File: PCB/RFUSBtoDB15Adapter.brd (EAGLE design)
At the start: 39 x 66 mm, 7 parts, among them J2 AVR_SPI_PROG_3X2NS

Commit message: New PCB
PCB updated
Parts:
- added C1: 0.1uf, Wurth_Elektronik_Passive_Capacitors_rev18b:WCAP-CSGP_0805_REFLOW
- added C2: 10uF, SparkFun-Capacitors:EIA3216
- added IC1: S-816A40AMC-BAPT2U, S-816A40AMC-BAPT2U:SOT95P275X130-5N
- added JP2: (no value), pinhead:1X01
- added LED: (no value), adafruit:LED3MM
- added PEM1, PEM2, PEM3, PEM4: KF2-M2, penn-engineering:KF2-M2
- added Q2: 2SA1213-Y(TE12L,F), 2SA1213YTE12LF:PW-MINI_TOS
- added R1: 33Ω, eagle-ltspice:R0805
- added SJ1, SJ2, SJ3: (no value), jumper:SJ
- moved 3.3V 3.81 mm to (38.1, 57.1)
- moved J2 3.81 mm to (8.89, 20.3)
- moved ARDUINO-ATMEGA328P 3.81 mm to (24.1, 38.1)
- moved DB15OUT 3.81 mm to (23.4, 71.2)
- moved JP3 3.81 mm to (21.6, 22.9)
- moved J1 3.81 mm to (36.8, 16.5)
- moved JP1 3.81 mm to (37.8, 64.1)
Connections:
- new net 5VREG: 3.3V.3, C1.1, C2.+, IC1.3, IC1.5, JP1.1, Q2.3, R1.2, SJ1.2, SJ3.1, SJ3.2
- new net BASE: IC1.1, Q2.1
- new net VBUS: C1.2, JP2.1, R1.1
- net 5VSG: now also IC1.4, Q2.2, SJ1.1, SJ2.1, SJ2.2; no longer 3.3V.3, J2.2, JP1.1
- net GND: now also C2.-, IC1.2
- net VCCIN: now also J2.2
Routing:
- net 5VREG: track 0.00 -> 142.7 mm
- net 5VSG: track 93.3 -> 28.0 mm, vias 3 -> 0
- net VCCIN: track 58.8 -> 93.3 mm
- net BASE: track 0.00 -> 28.1 mm
- net VBUS: track 0.00 -> 7.99 mm, vias 0 -> 1
- net BUT3: track 70.1 -> 74.2 mm
- net START: track 43.6 -> 41.0 mm
- net UP: track 62.5 -> 61.2 mm
- net BUT6: track 31.5 -> 32.5 mm
- net DOWN: track 39.1 -> 38.5 mm
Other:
- board size 39 x 66 mm -> 52.1 x 68.6 mm
- board text added: "For instructions access: github.com/Raphfriend/USB2DB15"
- board text removed: "https://github.com/Raphfriend/USB2DB15"

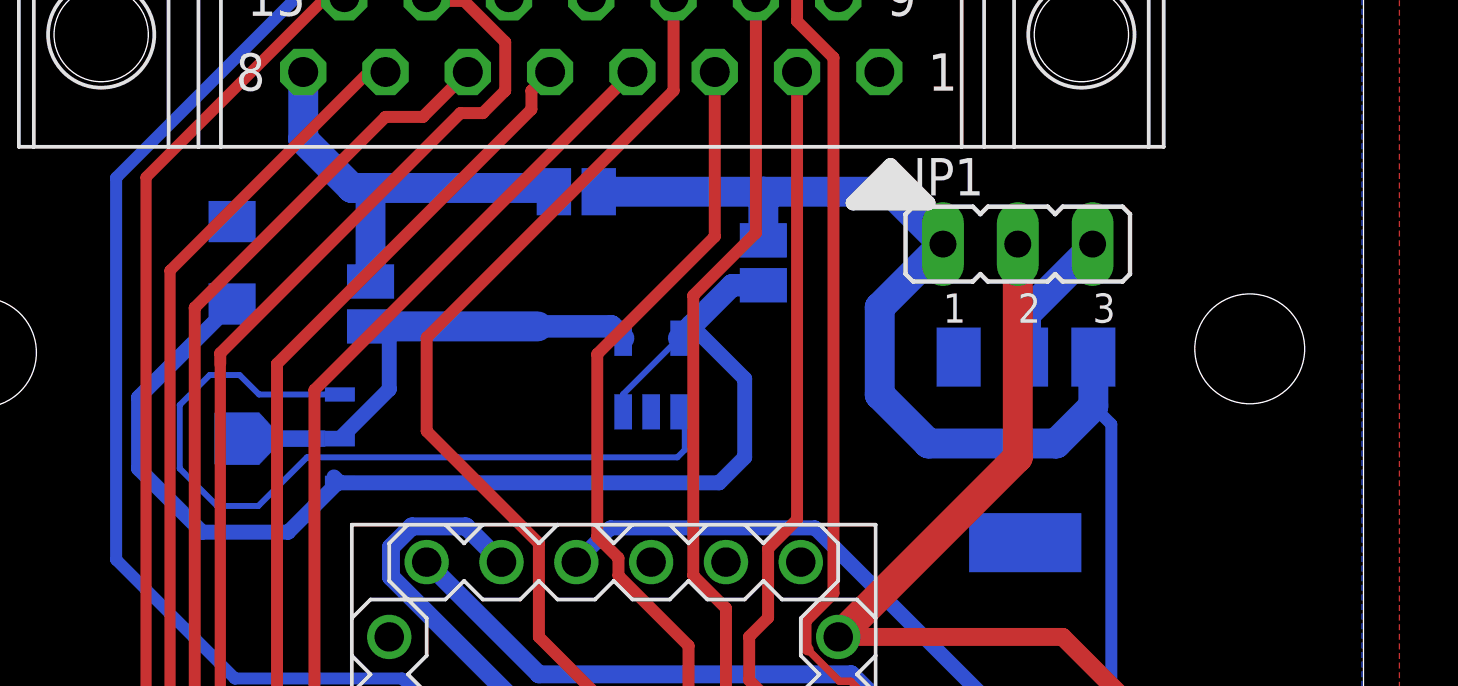
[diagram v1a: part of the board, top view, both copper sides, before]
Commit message: Update RFUSBtoDB15Adapter.brd
Changes on PCB
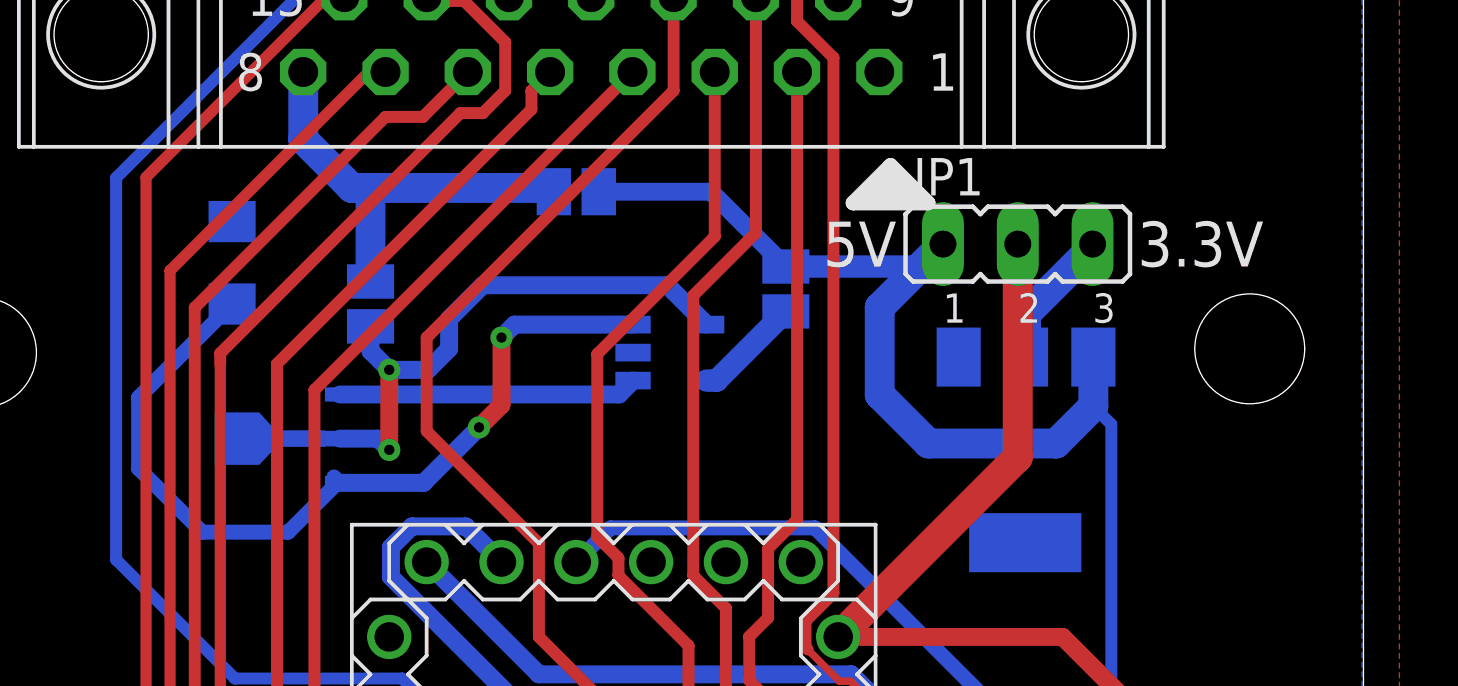
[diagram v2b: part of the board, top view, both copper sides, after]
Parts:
- moved SJ3 1.17 mm to (30.0, 62.6)
- moved IC1 0.99 mm to (26.0, 60.5), turned to 180 degrees
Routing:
- net BASE: track 28.1 -> 10.1 mm
- net 5VREG: track 142.7 -> 132.2 mm, vias 0 -> 2
- net 5VSG: track 28.0 -> 34.1 mm, vias 0 -> 2
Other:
- board text added: "3.3V"
- board text added: "5V"

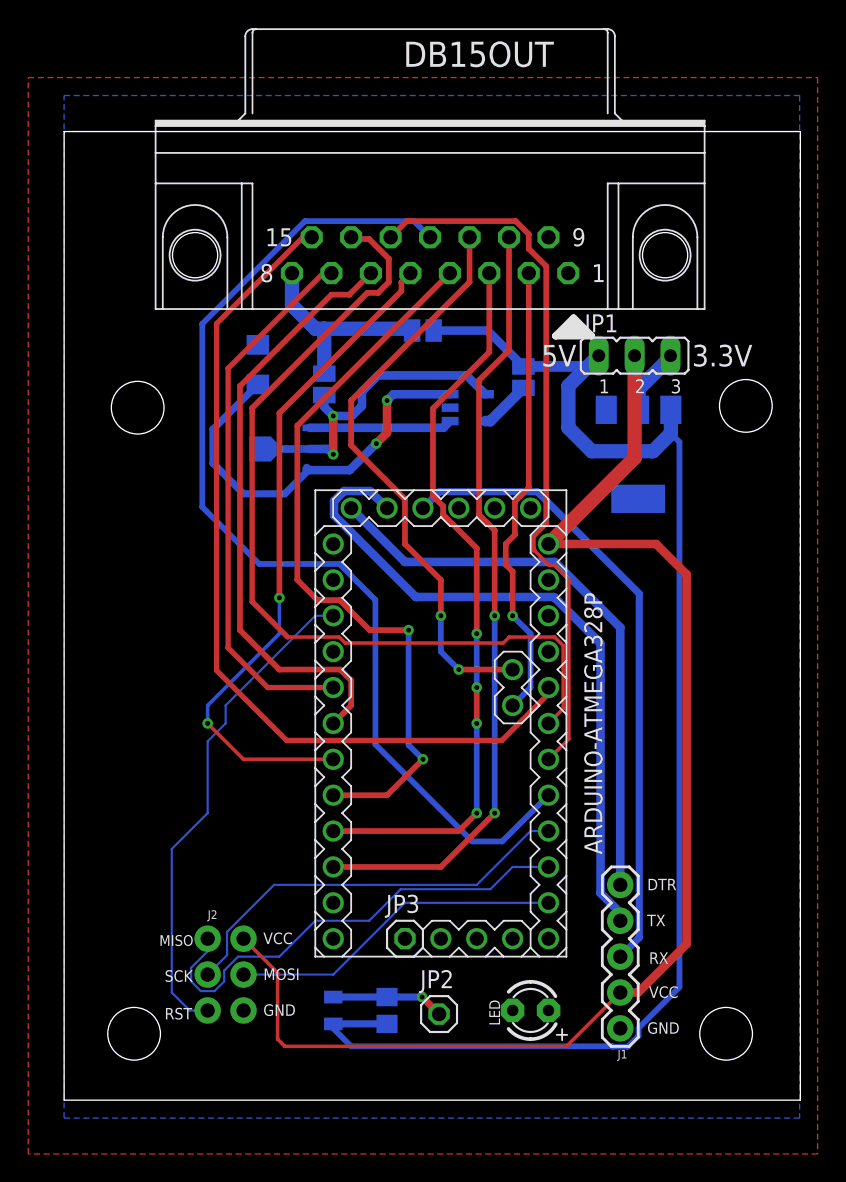
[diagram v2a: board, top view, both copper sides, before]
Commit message: Updates
Schematic, PCB and code updates.
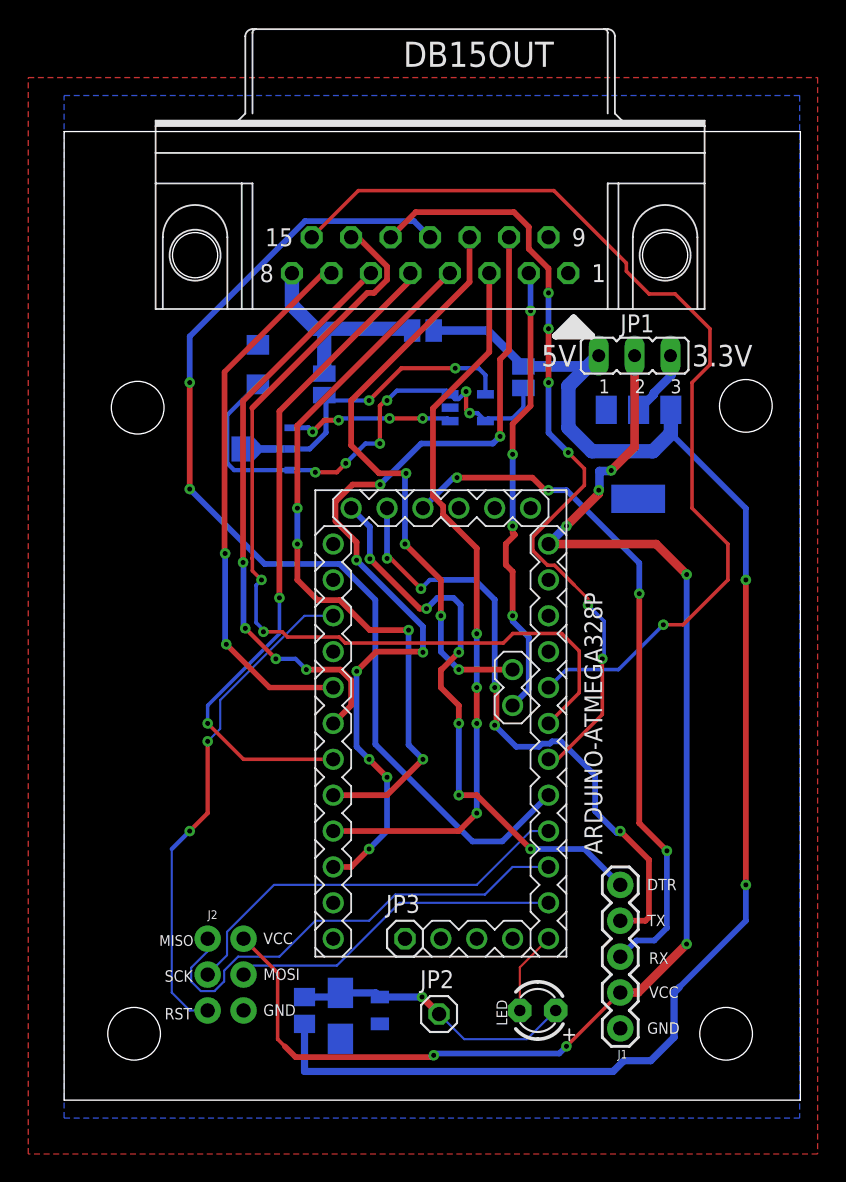
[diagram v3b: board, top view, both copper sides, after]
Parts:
- added C5: 4.7UF, resistor:B/3528-21W
- DB15OUT, J1, JP3: value (none) -> 0
- JP2: value (none) -> JP2
- moved R1 5.84 mm to (14.5, 17.8)
- moved C1 3.30 mm to (19.8, 17.8)
- moved Q2 1.27 mm to (11.8, 57.5)
- moved LED 0.51 mm to (31.0, 17.8)
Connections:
- new net LED: ARDUINO-ATMEGA328P.J6.12, LED.K
- new net VCC: ARDUINO-ATMEGA328P.J6.4
- net 5VREG: no longer C1.1
- net GND: now also C1.1, C5.-
- net VBUS: now also C5.+, LED.A
- net VCCIN: no longer ARDUINO-ATMEGA328P.J6.4
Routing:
- net VBUS: track 7.99 -> 20.1 mm
- net 5VREG: track 132.2 -> 141.9 mm, vias 2 -> 8
- net BUT5: track 55.1 -> 63.5 mm, vias 2 -> 8
- net UP: track 61.2 -> 69.2 mm, vias 0 -> 1
- net LED: track 0.00 -> 5.92 mm
- net BUT1: track 50.6 -> 56.2 mm, vias 0 -> 6
- net RX: track 45.0 -> 49.5 mm, vias 0 -> 4
- net TX: track 48.4 -> 44.9 mm, vias 0 -> 5
- net BASE: track 10.1 -> 11.8 mm, vias 0 -> 4
- net LEFT: track 62.0 -> 63.6 mm, vias 0 -> 2
- net START: track 41.0 -> 42.2 mm, vias 2 -> 4
- net RIGHT: track 42.8 -> 41.8 mm, vias 0 -> 4
- net VCCIN: track 93.3 -> 94.1 mm, vias 0 -> 7
- net BUT3: track 74.2 -> 74.8 mm, vias 0 -> 2
- net DTR: track 40.8 -> 41.2 mm, vias 0 -> 6
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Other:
- board text added: "+"
- board text added: "4.7uf"
- board text added: "USB2DB15 Adapter for Supergun/Neogeo 1.0 by Raph_friend"
- board text removed: "USB2DB15 Adapter for Supergun/Neogeo"
- board text removed: "by Raph_friend"

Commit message: PCB
Some changes
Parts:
- added LOGO1: OSHW-LOGOS, SparkFun-Aesthetics:OSHW-LOGO-S
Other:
- board text added: "Made in Brazil"
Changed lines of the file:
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@@
 <text x="18.415" y="19.558" size="0.6096" layer="26" rot="MR0">+</text>
 <text x="12.446" y="60.579" size="0.6096" layer="26" rot="MR0">+</text>
+<text x="25.146" y="41.91" size="1.778" layer="26" rot="MR270">Made in Brazil</text>
 </plain>
 <attributes>
@@
 <attribute name="VALUE" x="14.093" y="15.449" size="1.27" layer="28" rot="MR90"/>
 </element>
+<element name="LOGO1" library="SparkFun-Aesthetics" library_urn="urn:adsk.eagle:library:507" package="OSHW-LOGO-S" package3d_urn="urn:adsk.eagle:package:37099/1" value="OSHW-LOGOS" x="0.381" y="55.372" smashed="yes" rot="MR90"/>
 </elements>
 <signals>

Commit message: PCB
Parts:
- added S1: RS032G05A3SM-SPST-MOMENTARY-SWSMD-1101NE, BeagleBone_Blue_R3:TACTILE-SWITCH-1101NE
- renumbered JP3 to A4
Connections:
- net BUT6: now also A4.1
- net GND: now also S1.1; no longer ARDUINO-ATMEGA328P.J3.1
- net RESET: now also S1.2
- net START: now also ARDUINO-ATMEGA328P.J3.1
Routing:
- net START: track 42.2 -> 68.9 mm
- net BUT6: track 32.7 -> 56.0 mm
- net RESET: track 35.7 -> 40.8 mm
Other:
- board text added: "A4"
- board text added: "A5"
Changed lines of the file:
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@@
 <text x="12.446" y="60.579" size="0.6096" layer="26" rot="MR0">+</text>
 <text x="25.146" y="41.91" size="1.778" layer="26" rot="MR270">Made in Brazil</text>
+<text x="22.987" y="24.257" size="1.27" layer="25">A5</text>
+<text x="30.353" y="44.577" size="1.27" layer="25" rot="R180">A5</text>
+<text x="30.353" y="37.973" size="1.27" layer="25" rot="R180">A4</text>
 </plain>
 <attributes>
@@
 <attribute name="VALUE" x="4.953" y="24.13" size="0.6096" layer="27" font="vector" ratio="20" rot="R270"/>
 </element>
-<element name="JP3" library="pinhead" library_urn="urn:adsk.eagle:library:325" package="1X01" package3d_urn="urn:adsk.eagle:package:22485/2" value="0" x="21.59" y="22.86" smashed="yes">
-<attribute name="NAME" x="20.2438" y="24.6888" size="1.27" layer="25" ratio="10"/>
+<element name="A4" library="pinhead" library_urn="urn:adsk.eagle:library:325" package="1X01" package3d_urn="urn:adsk.eagle:package:22485/2" value="0" x="21.59" y="22.86" smashed="yes">
+<attribute name="NAME" x="20.4978" y="24.3078" size="1.27" layer="25" ratio="10"/>
 <attribute name="POPULARITY" value="64" x="21.59" y="22.86" size="1.778" layer="27" display="off"/>
 <attribute name="VALUE" x="20.32" y="19.685" size="1.27" layer="27"/>
@@
 </element>
 <element name="LOGO1" library="SparkFun-Aesthetics" library_urn="urn:adsk.eagle:library:507" package="OSHW-LOGO-S" package3d_urn="urn:adsk.eagle:package:37099/1" value="OSHW-LOGOS" x="0.381" y="55.372" smashed="yes" rot="MR90"/>
+<element name="S1" library="BeagleBone_Blue_R3" library_urn="urn:adsk.eagle:library:5828899" package="TACTILE-SWITCH-1101NE" package3d_urn="urn:adsk.eagle:package:5829833/3" value="RS032G05A3SM-SPST-MOMENTARY-SWSMD-1101NE" x="3.81" y="43.18" smashed="yes" rot="R270">
+<attribute name="NAME" x="5.81" y="46.18" size="0.762" layer="25" rot="R270"/>
+<attribute name="PROD_ID" value="SWCH-00815" x="3.81" y="43.18" size="1.778" layer="27" rot="R270" display="off"/>
+<attribute name="VALUE" x="1.11" y="46.18" size="0.762" layer="27" rot="R270"/>
+</element>
 </elements>
 <signals>
@@
 <wire x1="21.664375" y1="55.805625" x2="19.759375" y2="55.805625" width="0.4064" layer="1"/>
 <wire x1="19.759375" y1="55.805625" x2="17.78" y2="57.785" width="0.4064" layer="1"/>
+<contactref element="ARDUINO-ATMEGA328P" pad="J3.1"/>
+<wire x1="24.13" y1="22.86" x2="27.7034" y2="26.4334" width="0.254" layer="1"/>
+<wire x1="27.7034" y1="26.4334" x2="31.704859375" y2="26.4334" width="0.254" layer="1"/>
+<wire x1="31.704859375" y1="26.4334" x2="32.783403125" y2="27.51194375" width="0.254" layer="1"/>
+<wire x1="32.783403125" y1="27.51194375" x2="32.783403125" y2="30.90805625" width="0.254" layer="1"/>
+<wire x1="32.783403125" y1="30.90805625" x2="31.704859375" y2="31.9866" width="0.254" layer="1"/>
+<wire x1="31.704859375" y1="31.9866" x2="31.321940625" y2="31.9866" width="0.254" layer="1"/>
+<wire x1="31.321940625" y1="31.9866" x2="30.48" y2="32.828540625" width="0.254" layer="1"/>
+<wire x1="30.48" y1="32.828540625" x2="30.48" y2="40.64" width="0.254" layer="1"/>
+<wire x1="30.48" y1="40.64" x2="29.21" y2="41.91" width="0.254" layer="1"/>
 </signal>
 <signal name="BUT4">
@@
 <via x="29.21" y="57.15" extent="1-16" drill="0.35"/>
 <wire x1="29.21" y1="57.15" x2="29.21" y2="59.309" width="0.4064" layer="1"/>
+<contactref element="A4" pad="1"/>
+<wire x1="21.59" y1="22.86" x2="27.0980625" y2="28.3680625" width="0.254" layer="1"/>
+<wire x1="27.0980625" y1="28.3680625" x2="30.5680625" y2="28.3680625" width="0.254" layer="1"/>
+<wire x1="30.5680625" y1="28.3680625" x2="31.1376" y2="28.9376" width="0.254" layer="1"/>
+<wire x1="31.1376" y1="28.9376" x2="31.1376" y2="29.5480875" width="0.254" layer="1"/>
+<wire x1="31.1376" y1="29.5480875" x2="29.21" y2="31.4756875" width="0.254" layer="1"/>
+<wire x1="29.21" y1="31.4756875" x2="29.21" y2="39.37" width="0.254" layer="1"/>
 </signal>
 <signal name="GND">
 <contactref element="DB15OUT" pad="1"/>
 <contactref element="3.3V" pad="1"/>
-<contactref element="ARDUINO-ATMEGA328P" pad="J3.1"/>
 <contactref element="J1" pad="1"/>
 <contactref element="ARDUINO-ATMEGA328P" pad="J1.1"/>
@@
 <contactref element="C1" pad="1"/>
 <contactref element="C5" pad="-"/>
+<contactref element="S1" pad="1"/>
 </signal>
 <signal name="5VSG">
@@
 <wire x1="7.62" y1="31.75" x2="7.62" y2="36.83" width="0.3048" layer="1"/>
 <via x="7.62" y="36.83" extent="1-16" drill="0.35"/>
+<contactref element="S1" pad="2"/>
+<wire x1="7.62" y1="36.83" x2="7.01" y2="36.83" width="0.1524" layer="1"/>
+<wire x1="7.01" y1="36.83" x2="3.81" y2="40.03" width="0.1524" layer="1"/>
 </signal>
 <signal name="SCK">

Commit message: PCB
PCB design updated
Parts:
- removed JP1: (no value), jumper:JP2
- removed SJ3: (no value), jumper:SJ
- added C3, C4: 10uF, SparkFun-Capacitors:EIA3216
- R1: value 33Ω -> 80R; device eagle-ltspice:R0805 -> SparkFun-Resistors:0805
- moved J1 45.2 mm to (8.89, 52.1)
- moved S1 38.9 mm to (41.9, 35.6)
- moved J2 29.9 mm to (38.7, 21.2)
- moved Q2 21.9 mm to (22.9, 38.6), turned to 180 degrees
- moved C1 16.0 mm to (24.4, 33.1)
- moved C5 16.0 mm to (21.6, 32.8)
- moved C2 14.3 mm to (25.4, 62.0), turned to 180 degrees
- moved IC1 14.1 mm to (25.9, 46.4), turned to 90 degrees
- moved R1 13.7 mm to (27.9, 15.2), turned to 0 degrees
- moved PEM2 1.02 mm to (45.3, 16.0)
- moved PEM3 0.90 mm to (1.78, 60.3)
- moved PEM1 0.80 mm to (1.65, 15.9)
- moved PEM4 0.52 mm to (45.2, 60.5)
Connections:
- removed net VBUS: C1.2, C5.+, JP2.1, LED.A, R1.1
- removed net VCC: ARDUINO-ATMEGA328P.J6.4
- removed net VCCIN: ARDUINO-ATMEGA328P.J6.1, J1.2, J2.2, JP1.2
- new net 5VLED: LED.A, R1.1
- new net RAW: ARDUINO-ATMEGA328P.J6.1
- net 3.3V: now also ARDUINO-ATMEGA328P.J6.4, C4.+; no longer JP1.3
- net 5VREG: now also C1.2, C3.+, C5.+, J1.2, J2.2, JP2.1; no longer JP1.1, SJ3.1, SJ3.2
- net GND: now also C3.-, C4.-
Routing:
- net VCCIN: track 94.1 -> 0.00 mm, vias 7 -> 0
- net RX: track 49.5 -> 15.5 mm, vias 4 -> 1
- net TX: track 44.9 -> 15.2 mm, vias 5 -> 1
- net BUT3: track 74.8 -> 46.6 mm, vias 2 -> 0
- net DTR: track 41.2 -> 14.8 mm, vias 6 -> 1
- net MISO: track 33.2 -> 8.79 mm
- net VBUS: track 20.1 -> 0.00 mm, vias 1 -> 0
- net CREDIT: track 51.8 -> 69.9 mm, vias 4 -> 2
- net 3.3V: track 4.82 -> 22.7 mm
- net SCK: track 29.3 -> 11.6 mm
- net LEFT: track 63.6 -> 48.7 mm, vias 2 -> 1
- net START: track 68.9 -> 54.7 mm, vias 4 -> 1
- net MOSI: track 23.8 -> 9.99 mm
- net GND: track 0.00 -> 13.4 mm, vias 0 -> 5
- net 5VSG: track 34.2 -> 47.1 mm, vias 2 -> 3
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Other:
- board text removed: "3.3V"
- board text removed: "5V"

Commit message: PCB update
Small changes
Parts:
- moved JP2 9.30 mm to (19.1, 25.4)
- renumbered ARDUINO-ATMEGA328P to ARDUINO-MINIPRO
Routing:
- net 5VREG: track 143.4 -> 145.3 mm
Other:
- board text added: "ARDUINO PRO MINI"
- board text added: "RESET"
- board text removed: "RST"

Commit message: PCB Update
LED status and MEMORY RESET now supported
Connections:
- new net RESET_MEM: ARDUINO-MINIPRO.J3.2, S1.2
- net LED: now also ARDUINO-MINIPRO.J7.2; no longer ARDUINO-MINIPRO.J6.12
- net RESET: no longer S1.2
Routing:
- net RESET_MEM: track 0.00 -> 20.7 mm, vias 0 -> 2
- net RESET: track 48.9 -> 47.1 mm
- net LED: track 5.92 -> 4.65 mm
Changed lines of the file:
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@@
 <drawing>
 <settings>
-<setting alwaysvectorfont="yes"/>
+<setting alwaysvectorfont="no"/>
 <setting verticaltext="up"/>
 </settings>
@@
 <contactref element="ARDUINO-MINIPRO" pad="J7.10"/>
 <contactref element="J2" pad="5"/>
-<contactref element="S1" pad="2"/>
 <via x="39.37" y="33.02" extent="1-16" drill="0.35"/>
 <wire x1="32.19909375" y1="31.9358" x2="31.30090625" y2="31.9358" width="0.3556" layer="16"/>
@@
 <wire x1="39.37" y1="29.21" x2="40.64" y2="30.48" width="0.3556" layer="16"/>
 <via x="40.64" y="30.48" extent="1-16" drill="0.35"/>
-<wire x1="41.91" y1="31.75" x2="40.64" y2="30.48" width="0.3556" layer="1"/>
-<wire x1="39.37" y1="33.02" x2="40.64" y2="33.02" width="0.3556" layer="1"/>
-<wire x1="40.64" y1="33.02" x2="41.91" y2="31.75" width="0.3556" layer="1"/>
-<wire x1="40.64" y1="30.48" x2="41.91" y2="32.41" width="0" layer="19" extent="1-1"/>
+<wire x1="40.64" y1="30.48" x2="39.37" y2="31.75" width="0.3556" layer="1"/>
+<wire x1="39.37" y1="31.75" x2="39.37" y2="33.02" width="0.3556" layer="1"/>
 </signal>
 <signal name="SCK">
@@
 </signal>
 <signal name="LED">
-<contactref element="ARDUINO-MINIPRO" pad="J6.12"/>
 <contactref element="LED" pad="K"/>
 <wire x1="29.718" y1="17.78" x2="29.718" y2="19.558" width="0.3556" layer="1"/>
 <wire x1="29.718" y1="19.558" x2="31.75" y2="21.59" width="0.3556" layer="1"/>
-<wire x1="31.75" y1="21.59" x2="31.75" y2="22.86" width="0.3556" layer="1"/>
+<contactref element="ARDUINO-MINIPRO" pad="J7.2"/>
+<wire x1="16.51" y1="25.4" x2="29.718" y2="17.78" width="0" layer="19" extent="1-1"/>
 </signal>
 <signal name="RAW">
@@
 <wire x1="29.718" y1="15.24" x2="32.258" y2="17.78" width="0.508" layer="16"/>
 </signal>
+<signal name="RESET_MEM">
+<contactref element="ARDUINO-MINIPRO" pad="J3.2"/>
+<contactref element="S1" pad="2"/>
+<wire x1="41.91" y1="32.41" x2="41.25" y2="31.75" width="0.3556" layer="1"/>
+<wire x1="41.25" y1="31.75" x2="40.64" y2="31.75" width="0.3556" layer="1"/>
+<via x="40.64" y="31.75" extent="1-16" drill="0.35"/>
+<wire x1="40.64" y1="31.75" x2="39.37" y2="30.48" width="0.3556" layer="16"/>
+<wire x1="39.37" y1="30.48" x2="34.29" y2="30.48" width="0.3556" layer="16"/>
+<via x="34.29" y="30.48" extent="1-16" drill="0.35"/>
+<wire x1="34.29" y1="30.48" x2="33.02" y2="29.21" width="0.3556" layer="1"/>
+<wire x1="33.02" y1="29.21" x2="30.48" y2="29.21" width="0.3556" layer="1"/>
+<wire x1="30.48" y1="29.21" x2="29.21" y2="27.94" width="0.3556" layer="1"/>
+<wire x1="29.21" y1="27.94" x2="29.21" y2="25.4" width="0.3556" layer="1"/>
+<wire x1="29.21" y1="25.4" x2="26.67" y2="22.86" width="0.3556" layer="1"/>
+</signal>
 </signals>
